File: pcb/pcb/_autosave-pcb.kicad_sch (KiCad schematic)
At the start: 22 parts, among them J1 UART, J2 Barrel_Jack, J3 Stepper, SW1 RESET, SW2 FLASH, U1 ESP32-WROOM-32, U2 TSR_1-2433

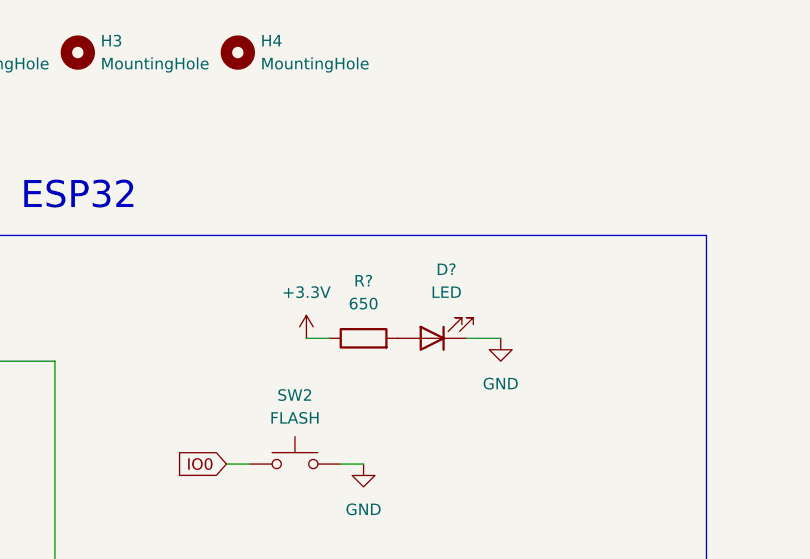
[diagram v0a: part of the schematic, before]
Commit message: Add power led
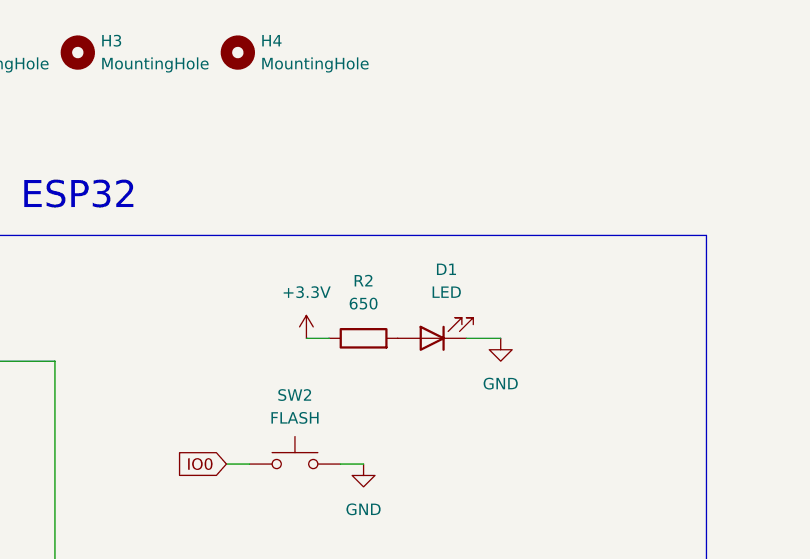
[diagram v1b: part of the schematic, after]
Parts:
- gave numbers to parts that had none: 2
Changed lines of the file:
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@@
   (symbol (lib_id "Device:LED") (at 109.22 59.69 180) (unit 1)
     (in_bom yes) (on_board yes) (fields_autoplaced)
-    (property "Reference" "D?" (id 0) (at 110.8075 52.07 0))
+    (property "Reference" "D1" (id 0) (at 110.8075 52.07 0))
     (property "Value" "LED" (id 1) (at 110.8075 54.61 0))
     (property "Footprint" "LED_SMD:LED_1206_3216Metric_Pad1.42x1.75mm_HandSolder" (id 2) (at 109.22 59.69 0)
@@
   (symbol (lib_id "Device:R") (at 101.6 59.69 90) (unit 1)
     (in_bom yes) (on_board yes) (fields_autoplaced)
-    (property "Reference" "R?" (id 0) (at 101.6 53.34 90))
+    (property "Reference" "R2" (id 0) (at 101.6 53.34 90))
     (property "Value" "650" (id 1) (at 101.6 55.88 90))
     (property "Footprint" "Resistor_SMD:R_1206_3216Metric_Pad1.30x1.75mm_HandSolder" (id 2) (at 101.6 61.468 90)
@@
   (symbol (lib_id "power:+3.3V") (at 95.25 59.69 0) (unit 1)
     (in_bom yes) (on_board yes) (fields_autoplaced)
-    (property "Reference" "#PWR?" (id 0) (at 95.25 63.5 0)
+    (property "Reference" "#PWR022" (id 0) (at 95.25 63.5 0)
       (effects (font (size 1.27 1.27)) hide)
     )
@@
   (symbol (lib_id "power:GND") (at 116.84 59.69 0) (unit 1)
     (in_bom yes) (on_board yes) (fields_autoplaced)
-    (property "Reference" "#PWR?" (id 0) (at 116.84 66.04 0)
+    (property "Reference" "#PWR023" (id 0) (at 116.84 66.04 0)
       (effects (font (size 1.27 1.27)) hide)
     )
@@
     )
     (path "/756a2c8a-40fc-4498-a763-fe751bbab7c7"
-      (reference "#PWR?") (unit 1) (value "+3.3V") (footprint "")
+      (reference "#PWR022") (unit 1) (value "+3.3V") (footprint "")
     )
     (path "/eafbdab6-0932-4d35-a03e-562d4b5965e8"
-      (reference "#PWR?") (unit 1) (value "GND") (footprint "")
+      (reference "#PWR023") (unit 1) (value "GND") (footprint "")
     )
     (path "/b03e052e-fb2e-4d5e-ae41-d75f2a2ed3e5"
@@
     )
     (path "/22353318-b610-462d-b49d-6e81aee2c761"
-      (reference "D?") (unit 1) (value "LED") (footprint "LED_SMD:LED_1206_3216Metric_Pad1.42x1.75mm_HandSolder")
+      (reference "D1") (unit 1) (value "LED") (footprint "LED_SMD:LED_1206_3216Metric_Pad1.42x1.75mm_HandSolder")
     )
     (path "/34fa3d54-c535-425c-b022-e1943d8d5f86"
@@
     )
     (path "/608f4001-cff0-46a4-9e8b-63808992aebd"
-      (reference "R?") (unit 1) (value "650") (footprint "Resistor_SMD:R_1206_3216Metric_Pad1.30x1.75mm_HandSolder")
+      (reference "R2") (unit 1) (value "650") (footprint "Resistor_SMD:R_1206_3216Metric_Pad1.30x1.75mm_HandSolder")
     )
     (path "/6efe0832-cbd1-4935-befc-012d6101080a"
